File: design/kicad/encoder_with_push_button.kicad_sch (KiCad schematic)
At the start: 4 parts

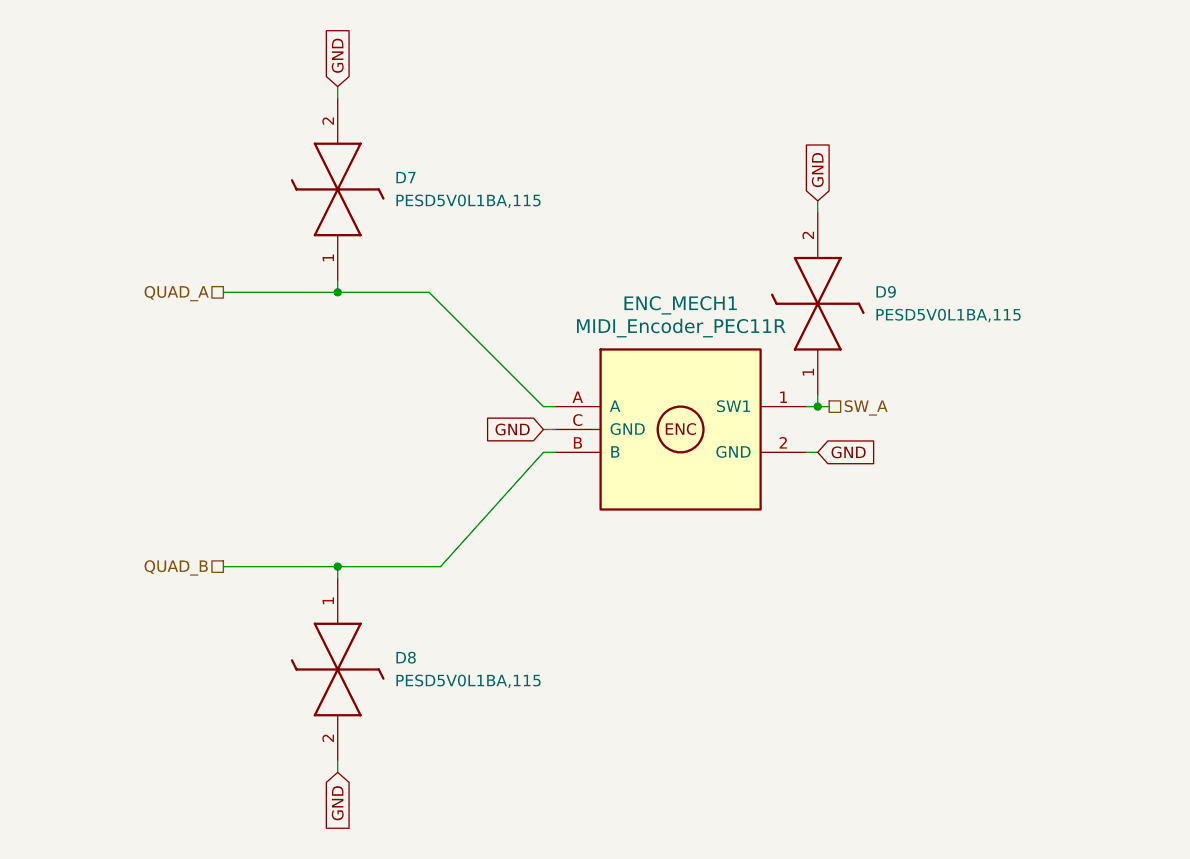
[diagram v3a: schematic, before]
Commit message: Fix reference labels and update wire connections in MIDI controller and multiplexer schematics
- Adjusted wire connection points in the MIDI controller schematic for better alignment.
- Updated label positions for various components in the MIDI controller schematic.
- Renamed reference designators for capacitors and power connections in the multiplexer schematic to maintain consistency.
- Corrected the reference designators for multiple components to reflect accurate labeling.
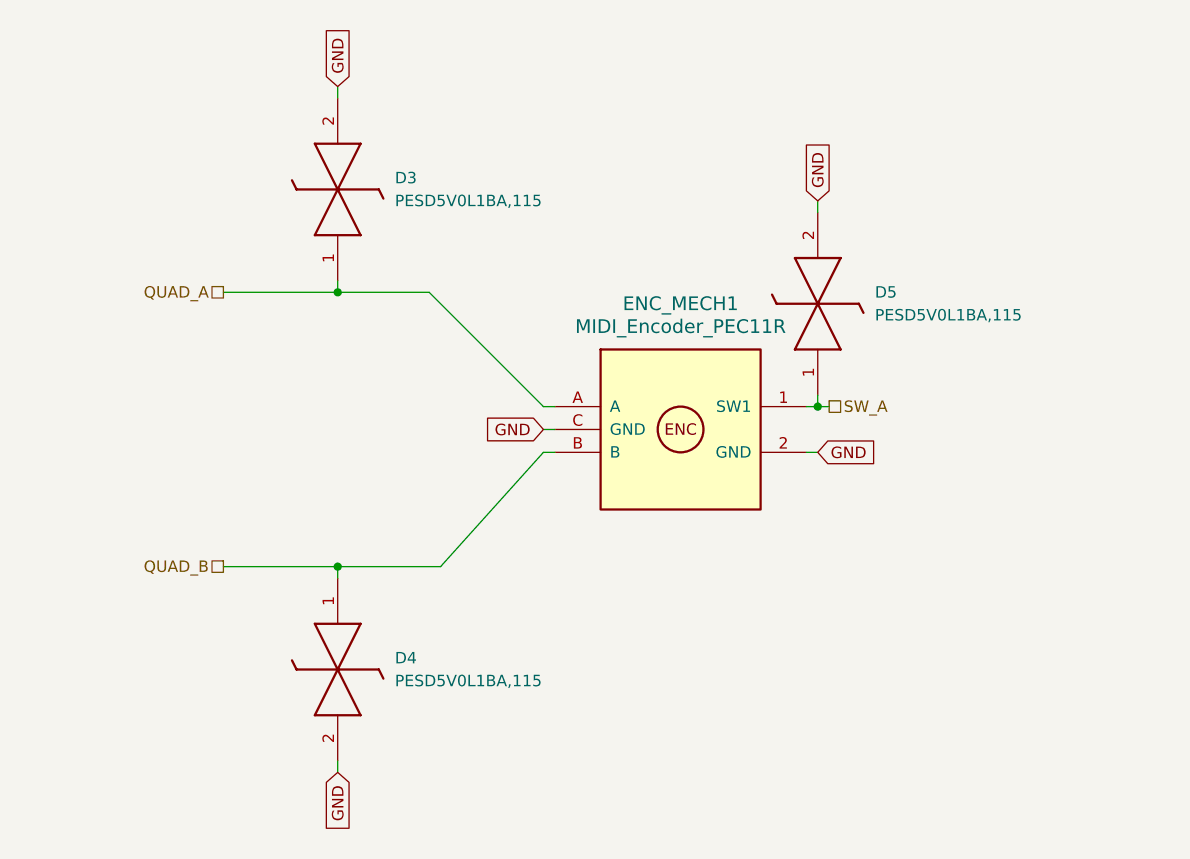
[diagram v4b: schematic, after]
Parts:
- renumbered D7 to D3, D8 to D4, D9 to D5
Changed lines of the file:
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@@
 		(dnp no)
 		(fields_autoplaced yes)
-		(property "Reference" "D7"
+		(property "Reference" "D3"
 			(at 69.85 48.2599 90)
 			(effects
@@
 			(project "midi_controller"
 				(path "/9e44e663-00d0-4f33-bf1f-c4ad78deb554/f2987add-55a5-4c89-9b33-db7ed86a6cdc"
-					(reference "D31")
+					(reference "D27")
 					(unit 1)
 				)
 				(path "/9e44e663-00d0-4f33-bf1f-c4ad78deb554/8b3bc88b-b526-44d8-9760-500b43fd5a71/0ace1318-b253-4d85-b784-aa61ad0f89cd"
-					(reference "D10")
+					(reference "D6")
 					(unit 1)
 				)
 				(path "/9e44e663-00d0-4f33-bf1f-c4ad78deb554/8b3bc88b-b526-44d8-9760-500b43fd5a71/1413c73c-0ad0-4a10-833c-ff3e4825f086"
-					(reference "D22")
+					(reference "D18")
 					(unit 1)
 				)
 				(path "/9e44e663-00d0-4f33-bf1f-c4ad78deb554/8b3bc88b-b526-44d8-9760-500b43fd5a71/24f763b3-d9d2-44ca-b0de-e5bd6d783cf4"
-					(reference "D25")
+					(reference "D21")
 					(unit 1)
 				)
 				(path "/9e44e663-00d0-4f33-bf1f-c4ad78deb554/8b3bc88b-b526-44d8-9760-500b43fd5a71/291f4e39-6718-4dda-83a6-20f8f943b75d"
-					(reference "D13")
+					(reference "D9")
 					(unit 1)
 				)
 				(path "/9e44e663-00d0-4f33-bf1f-c4ad78deb554/8b3bc88b-b526-44d8-9760-500b43fd5a71/3c9339b8-42f1-40cb-9183-aa88346af463"
-					(reference "D16")
+					(reference "D12")
 					(unit 1)
 				)
 				(path "/9e44e663-00d0-4f33-bf1f-c4ad78deb554/8b3bc88b-b526-44d8-9760-500b43fd5a71/4af660a9-1b0e-40bf-ba48-b976c7e464d4"
-					(reference "D19")
+					(reference "D15")
 					(unit 1)
 				)
 				(path "/9e44e663-00d0-4f33-bf1f-c4ad78deb554/8b3bc88b-b526-44d8-9760-500b43fd5a71/60e25267-b738-456c-86e0-26223ee5fe23"
-					(reference "D7")
+					(reference "D3")
 					(unit 1)
 				)
 				(path "/9e44e663-00d0-4f33-bf1f-c4ad78deb554/8b3bc88b-b526-44d8-9760-500b43fd5a71/761c51eb-8364-4d00-98cb-27a8734a6aa5"
-					(reference "D28")
+					(reference "D24")
 					(unit 1)
 				)
@@
 		(dnp no)
 		(fields_autoplaced yes)
-		(property "Reference" "D8"
+		(property "Reference" "D4"
 			(at 69.85 101.5999 90)
 			(effects
@@
 			(project "midi_controller"
 				(path "/9e44e663-00d0-4f33-bf1f-c4ad78deb554/f2987add-55a5-4c89-9b33-db7ed86a6cdc"
-					(reference "D32")
+					(reference "D28")
 					(unit 1)
 				)
 				(path "/9e44e663-00d0-4f33-bf1f-c4ad78deb554/8b3bc88b-b526-44d8-9760-500b43fd5a71/0ace1318-b253-4d85-b784-aa61ad0f89cd"
-					(reference "D11")
+					(reference "D7")
 					(unit 1)
 				)
 				(path "/9e44e663-00d0-4f33-bf1f-c4ad78deb554/8b3bc88b-b526-44d8-9760-500b43fd5a71/1413c73c-0ad0-4a10-833c-ff3e4825f086"
-					(reference "D23")
+					(reference "D19")
 					(unit 1)
 				)
 				(path "/9e44e663-00d0-4f33-bf1f-c4ad78deb554/8b3bc88b-b526-44d8-9760-500b43fd5a71/24f763b3-d9d2-44ca-b0de-e5bd6d783cf4"
-					(reference "D26")
+					(reference "D22")
 					(unit 1)
 				)
 				(path "/9e44e663-00d0-4f33-bf1f-c4ad78deb554/8b3bc88b-b526-44d8-9760-500b43fd5a71/291f4e39-6718-4dda-83a6-20f8f943b75d"
-					(reference "D14")
+					(reference "D10")
 					(unit 1)
 				)
 				(path "/9e44e663-00d0-4f33-bf1f-c4ad78deb554/8b3bc88b-b526-44d8-9760-500b43fd5a71/3c9339b8-42f1-40cb-9183-aa88346af463"
-					(reference "D17")
+					(reference "D13")
 					(unit 1)
 				)
 				(path "/9e44e663-00d0-4f33-bf1f-c4ad78deb554/8b3bc88b-b526-44d8-9760-500b43fd5a71/4af660a9-1b0e-40bf-ba48-b976c7e464d4"
-					(reference "D20")
+					(reference "D16")
 					(unit 1)
 				)
 				(path "/9e44e663-00d0-4f33-bf1f-c4ad78deb554/8b3bc88b-b526-44d8-9760-500b43fd5a71/60e25267-b738-456c-86e0-26223ee5fe23"
-					(reference "D8")
+					(reference "D4")
 					(unit 1)
 				)
 				(path "/9e44e663-00d0-4f33-bf1f-c4ad78deb554/8b3bc88b-b526-44d8-9760-500b43fd5a71/761c51eb-8364-4d00-98cb-27a8734a6aa5"
-					(reference "D29")
+					(reference "D25")
 					(unit 1)
 				)
@@
 		(dnp no)
 		(fields_autoplaced yes)
-		(property "Reference" "D9"
+		(property "Reference" "D5"
 			(at 123.19 60.9599 90)
 			(effects
@@
 			(project "midi_controller"
 				(path "/9e44e663-00d0-4f33-bf1f-c4ad78deb554/f2987add-55a5-4c89-9b33-db7ed86a6cdc"
-					(reference "D33")
+					(reference "D29")
 					(unit 1)
 				)
 				(path "/9e44e663-00d0-4f33-bf1f-c4ad78deb554/8b3bc88b-b526-44d8-9760-500b43fd5a71/0ace1318-b253-4d85-b784-aa61ad0f89cd"
-					(reference "D12")
+					(reference "D8")
 					(unit 1)
 				)
 				(path "/9e44e663-00d0-4f33-bf1f-c4ad78deb554/8b3bc88b-b526-44d8-9760-500b43fd5a71/1413c73c-0ad0-4a10-833c-ff3e4825f086"
-					(reference "D24")
+					(reference "D20")
 					(unit 1)
 				)
 				(path "/9e44e663-00d0-4f33-bf1f-c4ad78deb554/8b3bc88b-b526-44d8-9760-500b43fd5a71/24f763b3-d9d2-44ca-b0de-e5bd6d783cf4"
-					(reference "D27")
+					(reference "D23")
 					(unit 1)
 				)
 				(path "/9e44e663-00d0-4f33-bf1f-c4ad78deb554/8b3bc88b-b526-44d8-9760-500b43fd5a71/291f4e39-6718-4dda-83a6-20f8f943b75d"
-					(reference "D15")
+					(reference "D11")
 					(unit 1)
 				)
 				(path "/9e44e663-00d0-4f33-bf1f-c4ad78deb554/8b3bc88b-b526-44d8-9760-500b43fd5a71/3c9339b8-42f1-40cb-9183-aa88346af463"
-					(reference "D18")
+					(reference "D14")
 					(unit 1)
 				)
 				(path "/9e44e663-00d0-4f33-bf1f-c4ad78deb554/8b3bc88b-b526-44d8-9760-500b43fd5a71/4af660a9-1b0e-40bf-ba48-b976c7e464d4"
-					(reference "D21")
+					(reference "D17")
 					(unit 1)
 				)
 				(path "/9e44e663-00d0-4f33-bf1f-c4ad78deb554/8b3bc88b-b526-44d8-9760-500b43fd5a71/60e25267-b738-456c-86e0-26223ee5fe23"
-					(reference "D9")
+					(reference "D5")
 					(unit 1)
 				)
 				(path "/9e44e663-00d0-4f33-bf1f-c4ad78deb554/8b3bc88b-b526-44d8-9760-500b43fd5a71/761c51eb-8364-4d00-98cb-27a8734a6aa5"
-					(reference "D30")
-					(unit 1)
-				)
+					(reference "D26")
+					(unit 1)
+				)

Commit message: Update capacitor references in multiplexer schematic
Changed capacitor references from C11 to C42 and C12 to C43 in the multiplexer_CD74HC4067M schematic. Updated instances accordingly to maintain consistency in the design.
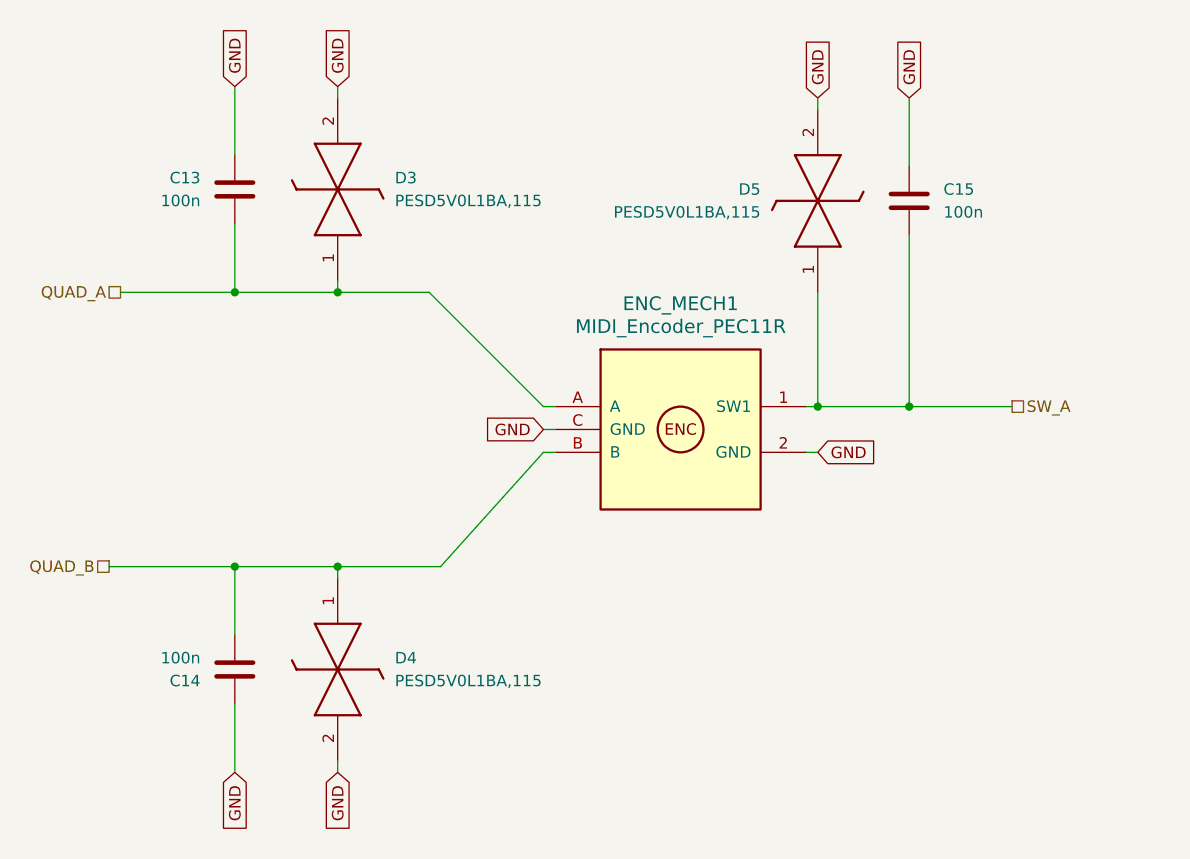
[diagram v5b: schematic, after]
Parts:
- added C13, C14, C15: 100n, Capacitor_SMD:C_0603_1608Metric, symbol Device:C
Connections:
- net GND: now also C13.1, C14.1, C15.1
- net QUAD_A: now also C13.2
- net QUAD_B: now also C14.2
- net SW_A: now also C15.2
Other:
- moved on the sheet: D5

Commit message: Update kicad binary files
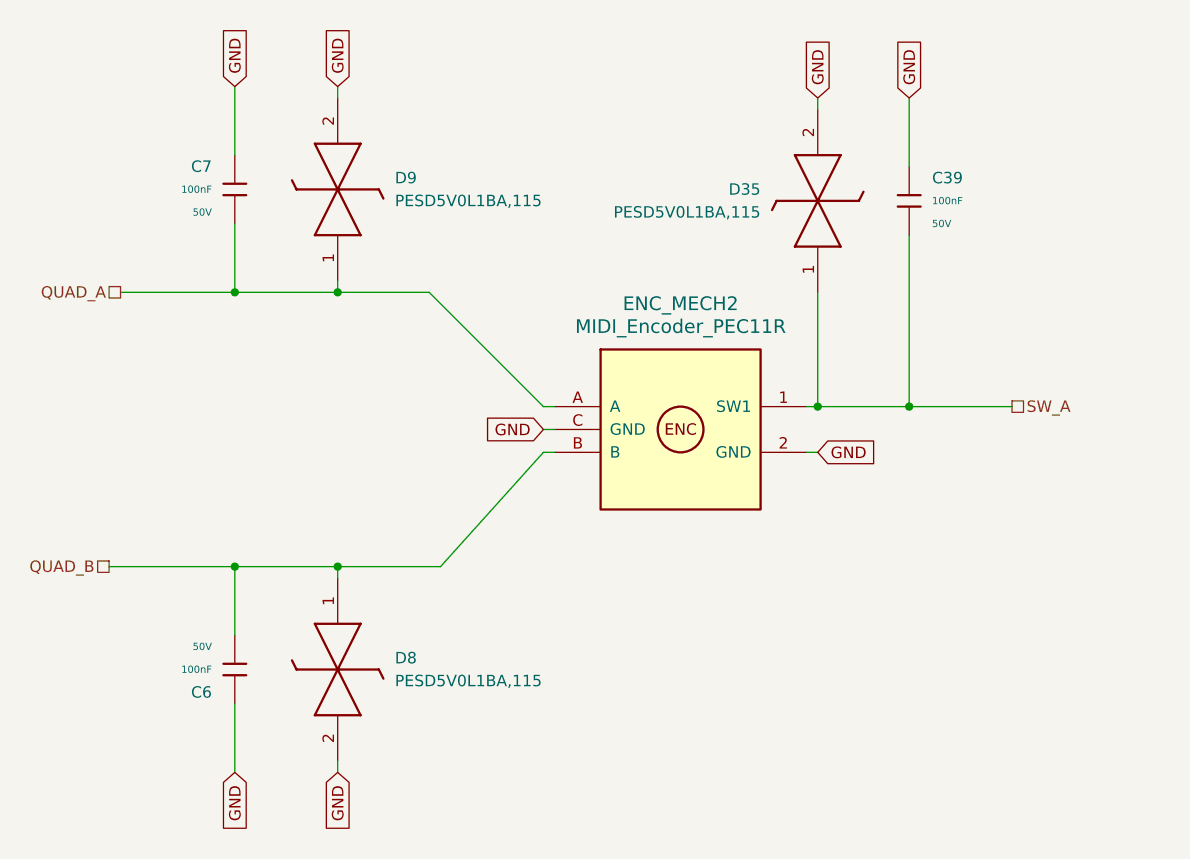
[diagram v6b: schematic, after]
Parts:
- removed C13, C14, C15: 100n, Capacitor_SMD:C_0603_1608Metric, symbol Device:C
- added C39, C6, C7: 100nF, PCM_JLCPCB:C_0603, symbol PCM_JLCPCB-Capacitors:0603,100nF
- D35: renamed from D5; LCSC (none) -> C85380
- D8: renamed from D4; LCSC (none) -> C85380
- D9: renamed from D3; LCSC (none) -> C85380
- ENC_MECH2: renamed from ENC_MECH1; now left out of the parts list
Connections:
- net GND: now also C39.1, C6.1, C7.1
- net QUAD_A: now also C7.2
- net QUAD_B: now also C6.2
- net SW_A: now also C39.2
